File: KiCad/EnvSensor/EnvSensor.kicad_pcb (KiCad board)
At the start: 2 copper layers, 120 x 100 mm, 90 parts, among them J1 SWD, J2 I2C, J3 USB_B_Micro, J4 Barrel_Jack, J5 Micro_SD_Card, P1 USB_C_Plug_USB2.0, Q1 IRLML2502, Q2 IRF7404, Q3 SQJB80EP, SW1 SW_Push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

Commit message: Last pcb fixes
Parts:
- P1: footprint Connector_USB:USB_C_Receptacle_Amphenol_12401610E4-2A -> JPConnectors:USB_C_Receptacle_Adam_Tech; moved to B.Cu
- R11: moved to B.Cu
- moved P1 14.2 mm to (21.0, 49.3), turned to 90 degrees
- moved D4 6.40 mm to (17.2, 65.8)
- moved D3 6.40 mm to (17.2, 59.2)
- moved D7 6.40 mm to (19.2, 67.2)
- moved D6 6.40 mm to (19.2, 60.6)
- moved R20 6.40 mm to (21.8, 65.8)
- moved R11 6.21 mm to (21.4, 59.2)
- moved J3 3.47 mm to (16.5, 36.0)
- moved J4 3.40 mm to (17.0, 36.0)
- moved C18 1.00 mm to (53.0, 45.3)
- moved J5 1.00 mm to (24.2, 83.8)
- moved Q2 0.60 mm to (47.5, 44.4)
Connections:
- D4 pad 2: VBUS -> Net-(C11-Pad1)
- D7 pad 2: VBUS -> Net-(C11-Pad1)
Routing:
- net VBUS: track 82.9 -> 64.7 mm, vias 3 -> 6
- net Net-(C11-Pad1): track 36.5 -> 52.7 mm
- net GND: track 221.3 -> 212.2 mm, vias 74 -> 69
- net Net-(R20-Pad1): track 29.4 -> 35.9 mm
- net SCK: track 90.6 -> 85.8 mm, vias 0 -> 1
- net MOSI: track 97.7 -> 93.6 mm
- net SDA: track 135.1 -> 138.6 mm
- net NRST: track 66.2 -> 68.6 mm
- net +BATT: track 125.8 -> 127.5 mm, vias 3 -> 4
- net +3V3: track 370.5 -> 371.0 mm, vias 16 -> 17
- net -BATT: track 125.7 -> 125.9 mm, vias 7 -> 6
- added copper zone on F.Cu, net GND
- added copper zone on F.Cu, net Net-(P1-PadS1)
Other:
- outline, holes or cut-outs redrawn
- board text added: "BME280"
- board text added: "BUSY"
- board text added: "CD"
- board text added: "ESP-12S"
- board text added: "Environmental Sensors, v1 JP, 2020.11.4"
- board text added: "HIH8121"
- board text added: "MOSI"
- board text added: "RESET"
- board text added: "SCD30"
- board text added: "SCK"
- board text added: "SELECT"
- board text removed: "Environmental Sensors, v1 JP, 2020.10.26"

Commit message: Faster eInk display transfer, faster I2C
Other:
- board text added: "J1 on the wrong side"
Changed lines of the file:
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@@
   (general
     (thickness 1.6)
-    (drawings 52)
+    (drawings 53)
     (tracks 1049)
     (zones 0)
@@
   )
   (setup
-    (last_trace_width 2)
+    (last_trace_width 0.28)
     (user_trace_width 0.28)
     (user_trace_width 0.4)
@@
     )
   )
+  (gr_text "J1 on the wrong side" (at -13.6 59.2) (layer Dwgs.User)
+    (effects (font (size 1.5 1.5) (thickness 0.3)))
+  )
   (gr_text BUSY (at 26.8 70.6) (layer F.SilkS)
     (effects (font (size 1.2 1.2) (thickness 0.2)) (justify left))
@@
   (segment (start 17.4025 58.06) (end 17.2 58.2625) (width 0.4) (layer F.Cu) (net 8))
   (segment (start 19.2 58.06) (end 17.4025 58.06) (width 0.4) (layer F.Cu) (net 8))
+  (segment (start 17.2025 64.66) (end 17 64.8625) (width 0.4) (layer F.Cu) (net 8))
+  (segment (start 19.2 64.66) (end 17.2025 64.66) (width 0.4) (layer F.Cu) (net 8))
+  (segment (start 17.1375 58.2) (end 17.2 58.2625) (width 0.4) (layer F.Cu) (net 8))
+  (segment (start 16.2625 64.8625) (end 15.8 64.4) (width 0.4) (layer F.Cu) (net 8))
+  (segment (start 17 64.8625) (end 16.2625 64.8625) (width 0.4) (layer F.Cu) (net 8))
+  (segment (start 15.8 64.4) (end 15.8 58.8) (width 0.4) (layer F.Cu) (net 8))
+  (segment (start 15.8 58.8) (end 16.4 58.2) (width 0.4) (layer F.Cu) (net 8))
+  (segment (start 16.4 58.2) (end 17.1375 58.2) (width 0.4) (layer F.Cu) (net 8))
+  (segment (start 24.3 50.2) (end 34.8 50.2) (width 0.4) (layer F.Cu) (net 8))
+  (segment (start 35.85 49.15) (end 37.5 49.15) (width 0.4) (layer F.Cu) (net 8))
+  (segment (start 22.8 51.7) (end 24.3 50.2) (width 0.4) (layer F.Cu) (net 8))
+  (segment (start 20.84 58.06) (end 22.8 56.1) (width 0.4) (layer F.Cu) (net 8))
+  (segment (start 34.8 50.2) (end 35.85 49.15) (width 0.4) (layer F.Cu) (net 8))
+  (segment (start 22.8 56.1) (end 22.8 51.7) (width 0.4) (layer F.Cu) (net 8))
+  (segment (start 19.2 58.06) (end 20.84 58.06) (width 0.4) (layer F.Cu) (net 8))
+  (segment (start 39.55 49.15) (end 37.5 49.15) (width 1) (layer F.Cu) (net 8))
+  (segment (start 42.3 49.6) (end 40 49.6) (width 1) (layer F.Cu) (net 8))
+  (segment (start 40 49.6) (end 39.55 49.15) (width 1) (layer F.Cu) (net 8))
   (segment (start 64.4625 81.325) (end 64.6 81.1875) (width 0.28) (layer F.Cu) (net 9))
   (segment (start 64.4625 81.9375) (end 63 81.9375) (width 0.4) (layer F.Cu) (net 9))
@@
   (segment (start 106.2 107.9375) (end 108.2 107.9375) (width 0.28) (layer F.Cu) (net 16))
   (segment (start 17 30.25) (end 23 30.25) (width 1) (layer B.Cu) (net 17))
-  (segment (start 17.2025 64.66) (end 17 64.8625) (width 0.4) (layer F.Cu) (net 8))
-  (segment (start 19.2 64.66) (end 17.2025 64.66) (width 0.4) (layer F.Cu) (net 8))
-  (segment (start 17.1375 58.2) (end 17.2 58.2625) (width 0.4) (layer F.Cu) (net 8))
-  (segment (start 16.2625 64.8625) (end 15.8 64.4) (width 0.4) (layer F.Cu) (net 8))
-  (segment (start 17 64.8625) (end 16.2625 64.8625) (width 0.4) (layer F.Cu) (net 8))
-  (segment (start 15.8 64.4) (end 15.8 58.8) (width 0.4) (layer F.Cu) (net 8))
-  (segment (start 15.8 58.8) (end 16.4 58.2) (width 0.4) (layer F.Cu) (net 8))
-  (segment (start 16.4 58.2) (end 17.1375 58.2) (width 0.4) (layer F.Cu) (net 8))
-  (segment (start 24.3 50.2) (end 34.8 50.2) (width 0.4) (layer F.Cu) (net 8))
-  (segment (start 35.85 49.15) (end 37.5 49.15) (width 0.4) (layer F.Cu) (net 8))
-  (segment (start 22.8 51.7) (end 24.3 50.2) (width 0.4) (layer F.Cu) (net 8))
-  (segment (start 20.84 58.06) (end 22.8 56.1) (width 0.4) (layer F.Cu) (net 8))
-  (segment (start 34.8 50.2) (end 35.85 49.15) (width 0.4) (layer F.Cu) (net 8))
-  (segment (start 22.8 56.1) (end 22.8 51.7) (width 0.4) (layer F.Cu) (net 8))
-  (segment (start 19.2 58.06) (end 20.84 58.06) (width 0.4) (layer F.Cu) (net 8))
-  (segment (start 39.55 49.15) (end 37.5 49.15) (width 1) (layer F.Cu) (net 8))
-  (segment (start 42.3 49.6) (end 40 49.6) (width 1) (layer F.Cu) (net 8))
-  (segment (start 40 49.6) (end 39.55 49.15) (width 1) (layer F.Cu) (net 8))
   (segment (start 21.117998 47.925) (end 21.675 47.925) (width 0.28) (layer B.Cu) (net 17))
   (segment (start 20.867998 48.175) (end 21.117998 47.925) (width 0.28) (layer B.Cu) (net 17))

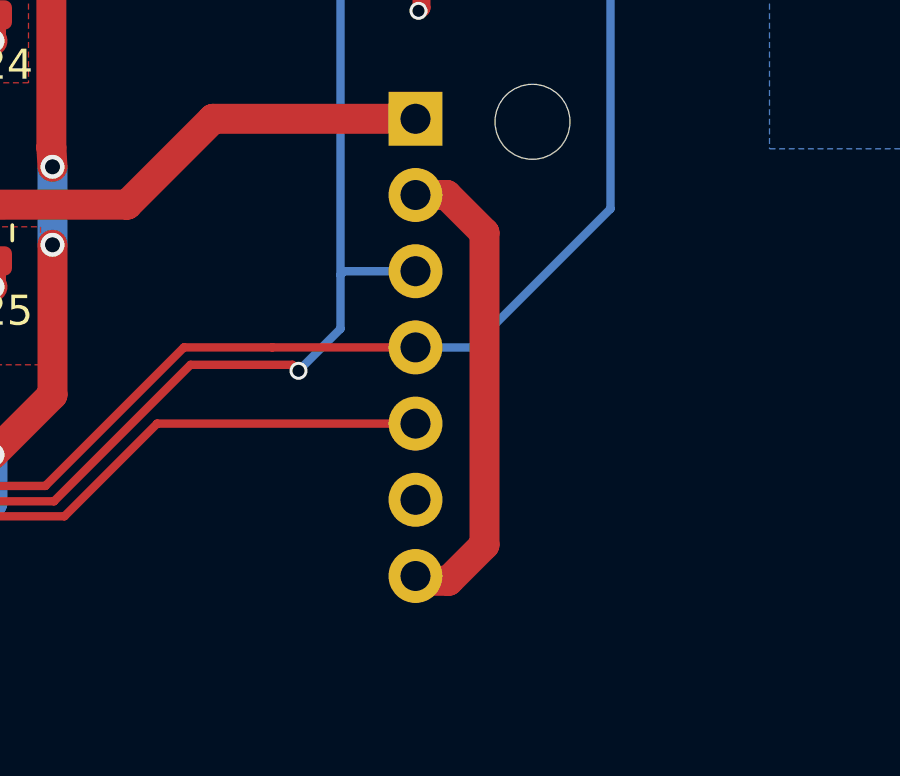
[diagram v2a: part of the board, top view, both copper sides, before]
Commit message: Single buffer fix. Retry code'
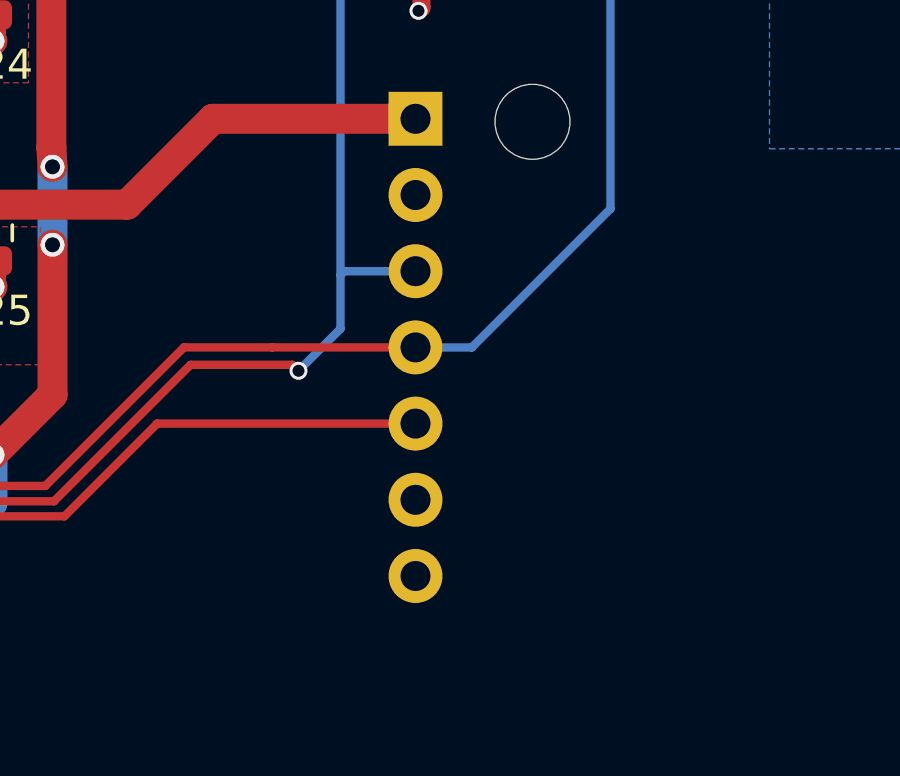
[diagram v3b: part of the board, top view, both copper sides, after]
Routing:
- net GND: track 212.2 -> 196.1 mm
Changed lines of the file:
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@@
     (thickness 1.6)
     (drawings 53)
-    (tracks 1049)
+    (tracks 1043)
     (zones 0)
     (modules 90)
@@
   (segment (start 70 75.4) (end 70.326 75.074) (width 0.28) (layer F.Cu) (net 84))
   (segment (start 68.826 75.226) (end 69 75.4) (width 0.28) (layer F.Cu) (net 84))
-  (segment (start 108.66 67.4) (end 108.5 67.24) (width 1) (layer F.Cu) (net 84))
-  (segment (start 109.54 54.54) (end 110.8 55.8) (width 1) (layer F.Cu) (net 84))
-  (segment (start 108.5 54.54) (end 109.54 54.54) (width 1) (layer F.Cu) (net 84))
-  (segment (start 109.6 67.4) (end 108.66 67.4) (width 1) (layer F.Cu) (net 84))
-  (segment (start 110.8 55.8) (end 110.8 66.2) (width 1) (layer F.Cu) (net 84))
-  (segment (start 110.8 66.2) (end 109.6 67.4) (width 1) (layer F.Cu) (net 84))
   (segment (start 48.4375 55.5) (end 49.25 55.5) (width 0.4) (layer F.Cu) (net 84))
   (segment (start 50.1875 54.5625) (end 50.1875 53.5) (width 0.4) (layer F.Cu) (net 84))
